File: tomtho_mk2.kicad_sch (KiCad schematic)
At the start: 173 parts, among them J1 USB-C, J2 BATTERY, J3 TRACKPAD, Q1 AO3401A, SW1 SKRAAWE010, SW10 SKRAAWE010, SW11 SKRAAWE010, SW12 SKRAAWE010, SW13 SKRAAWE010, SW14 SKRAAWE010, SW15 SKRAAWE010, SW16 SKRAAWE010, SW17 SKRAAWE010, SW18 SKRAAWE010, SW19 SKRAAWE010, SW2 SKRAAWE010, SW20 SKRAAWE010, SW21 SKRAAWE010, SW22 SKRAAWE010, SW23 SKRAAWE010, SW24 SKRAAWE010, SW25 SKRAAWE010, SW26 SKRAAWE010, SW27 SKRAAWE010, SW28 SKRAAWE010, SW29 SKRAAWE010, SW3 SKRAAWE010, SW30 SKRAAWE010, SW31 SKRAAWE010, SW32 SKRAAWE010, SW33 SKRAAWE010, SW34 SKRAAWE010, SW35 SKRAAWE010, SW36 SKRAAWE010, SW37 SKRAAWE010, SW38 SKRAAWE010, SW39 SKRAAWE010, SW4 SKRAAWE010, SW40 SKRAAWE010, SW41 SKRAAWE010, SW42 SKRAAWE010, SW43 SKRAAWE010, SW44 SKRAAWE010, SW45 SKRAAWE010, SW46 SKRAAWE010, SW47 SKRAAWE010, SW48 SKRAAWE010, SW49 SKRAAWE010, SW5 SKRAAWE010, SW50 SKRAAWE010, SW51 SKRAAWE010, SW52 SKRAAWE010, SW53 SKRAAWE010, SW54 SKRAAWE010, SW55 SKRAAWE010, SW56 SKRAAWE010, SW57 SKRAAWE010, SW58 SKRAAWE010, SW59 SKRAAWE010, SW6 SKRAAWE010, SW60 SKRAAWE010, SW61 SKRAAWE010, SW62 SKRAAWE010, SW63 SKRAAWE010, SW64 SKRAAWE010, SW65 SKRAAWE010, SW66 RESET, SW67 POWER, SW7 SKRAAWE010, SW8 SKRAAWE010, SW9 SKRAAWE010, U1 MDBT50Q-1MV2, U2 USBLC6-2SC6, U3 MCP73831

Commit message: mk2: schematic text layout fixes
Co-Authored-By: Claude Opus 5.5 <noreply@anthropic.com>
Claude-Session: https://claude.ai/code/session_014QKLhpB6tKWk1p8Y7v384p
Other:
- note added: "BT 切替"
- note added: "Battery 1S LiPo (protected)"
- note added: "Charger MCP73831 Ichg = 1000V / R3 = 100 mA LED1 = charging (VBUS powered)"
- note added: "Enter L1"
- note added: "GPIO map (ZMK, diode-direction = col2row) rows: ROW0=P1.10, ROW1=P1.11, ROW2=P1.13, ROW3=P1.15, ROW4=P0.29/AIN5, ROW5=P0.31/AIN7 cols: COL0=P0.30/AIN6, COL1=P0.27, COL2=P0.04/AIN2, COL3=P0.06, COL4=P0.08, COL5=P1.09 COL6=P0.24, COL7=P0.22, COL8=P0.20, COL9=P0.17, COL10=P0.15, COL11=P0.13 LED (active low): LED_BT1=P1.12, LED_BT2=P1.14, LED_BT3=P0.03/AIN1, LED_PWR_G=P0.02/AIN0, LED_PWR_R=P0.28/AIN4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"
- note added: "Indicator LEDs: bicolour, anode = VDD, GPIO sinks (active low) LED2-4 = BT1-3 (green die) / LED5 = power (green OK, red < 20 %)"
- note added: "Load sharing (AN1149) USB -> D66, battery -> Q1 SW67: VSYS -> VDDH"
- note added: "Space L2"
- note added: "Trackpad board (IQS550) FPC 6P 0.5 mm, I2C pull-ups here"
- note added: "tomtho-slim mk2 - 65 keys, roBa-style half stagger, centre trackpad (IQS550 on a separate board) ALPS SKRA 6.2mm / 18.5 x 18 mm pitch / nRF52840 (Raytac MDBT50Q-1MV2, TELEC) / 1S LiPo + USB-C / ZMK"
- note added: "変換 L6"
- note added: "無変換 L3"
- note removed: "BT\n切替"
- note removed: "Battery (1S LiPo, protected cell)"
- note removed: "Charger MCP73831: Ichg = 1000V / R3 = 100 mA\nLED1 lights while charging (VBUS powered)"
- note removed: "Enter\nL1"
- note removed: "GPIO map (ZMK, diode-direction = col2row)\nrows: ROW0=P1.10, ROW1=P1.11, ROW2=P1.13, ROW3=P1.15, ROW4=P0.29/AIN5, ROW5=P0.31/AIN7\ncols: COL0=P0.30/AIN6, COL1=P0.27, COL2=P0.04/AIN2, COL3=P0.06, COL4=P0.08, COL5=P1.09, COL6=P0.24, COL7=P0.22, COL8=P0.20, COL9=P0.17, COL10=P0.15, COL11=P0.13\nLED (active low): LED_BT1=P1.12, LED_BT2=P1.14, LED_BT3=P0.03/AIN1, LED_PWR_G=P0.02/AIN0, LED_PWR_R=P0.28/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"
- note removed: "Indicator LEDs (bicolour, common anode = VDD, GPIO sinks, active low)\nLED2-4 = BT1-3 (green die), LED5 = power (green OK / red < 20 %)"
- note removed: "Load sharing (AN1149): USB -> D66, else battery -> Q1\nPower switch SW67: VSYS -> VDDH"
- note removed: "Space\nL2"
- note removed: "Trackpad board (IQS550) via FPC 6P 0.5 mm, I2C pull-ups on this board"
- note removed: "tomtho-slim mk2 - 65 keys, roBa-style half stagger, centre trackpad (IQS550 on a separate board)\nALPS SKRA 6.2mm / 18.5 x 18 mm pitch / nRF52840 (Raytac MDBT50Q-1MV2, TELEC) / 1S LiPo + USB-C / ZMK"
- note removed: "変換\nL6"
- note removed: "無変換\nL3"

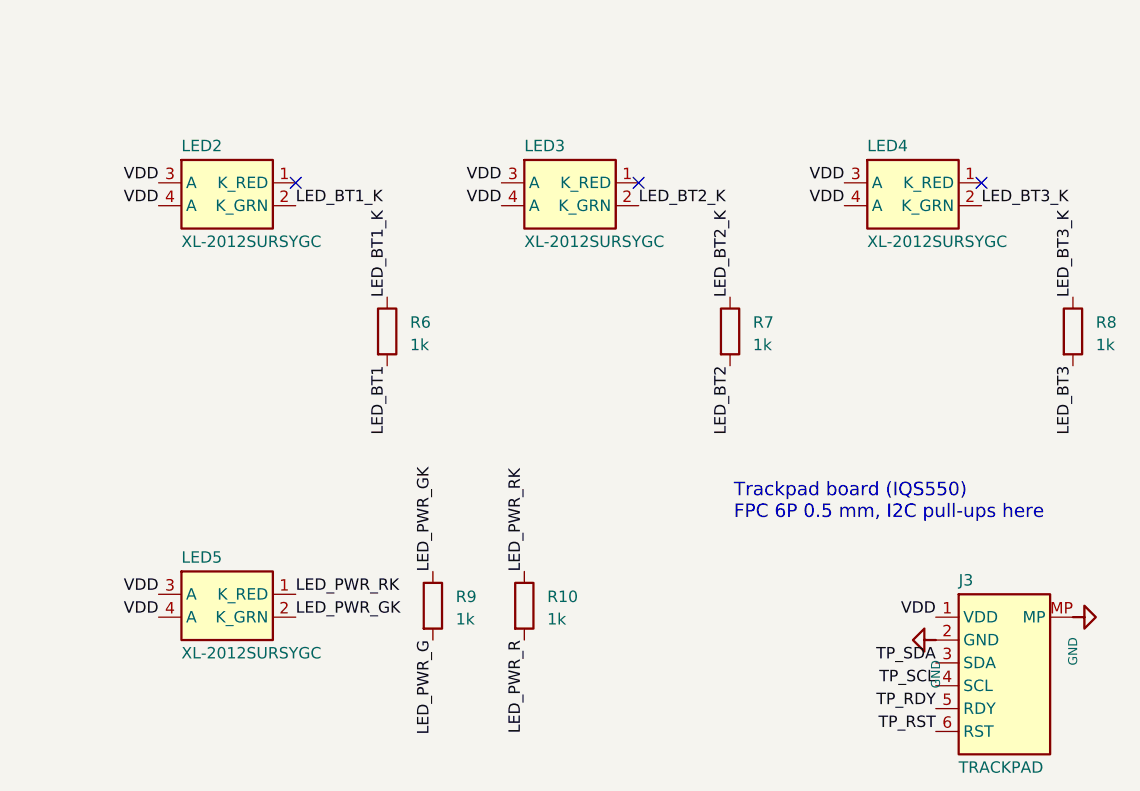
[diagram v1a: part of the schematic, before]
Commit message: mk2: PCB placement (all 173 parts, 0 courtyard overlaps), real LED pin map, top-mount USB-C, local KiCad DRC + Freerouting pipeline
Co-Authored-By: Claude Opus 5.5 <noreply@anthropic.com>
Claude-Session: https://claude.ai/code/session_014QKLhpB6tKWk1p8Y7v384p
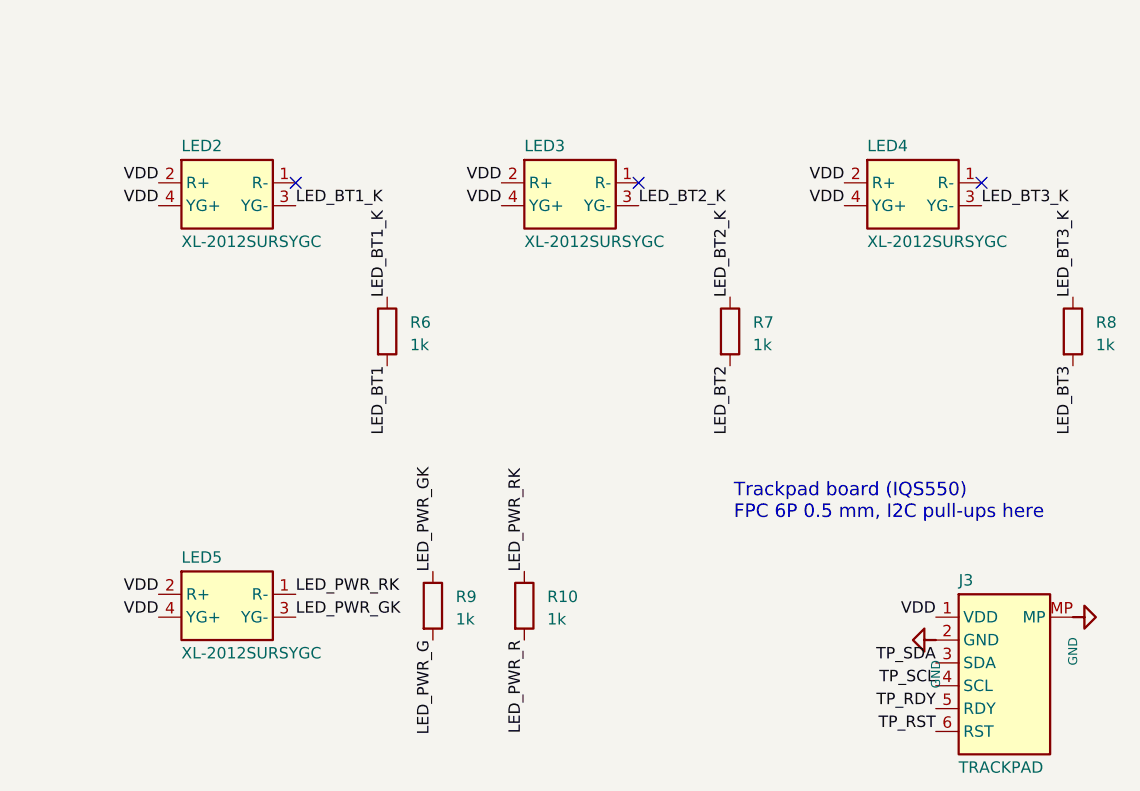
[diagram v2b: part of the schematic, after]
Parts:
- J1: footprint tomtho_mk2:USB_C_SHOUHAN_16P_CB1.6 -> tomtho_mk2:USB_C_HRO_TYPE-C-31-M-12; LCSC C2906290 -> C165948; MPN TYPE-C 16P CB1.6 073 -> TYPE-C-31-M-12
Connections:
- net LED_BT1_K: now also LED2.3 (YG-); no longer LED2.2 (K_GRN)
- net LED_BT2_K: now also LED3.3 (YG-); no longer LED3.2 (K_GRN)
- net LED_BT3_K: now also LED4.3 (YG-); no longer LED4.2 (K_GRN)
- net LED_PWR_GK: now also LED5.3 (YG-); no longer LED5.2 (K_GRN)
- net VDD: now also LED2.2 (R+), LED3.2 (R+), LED4.2 (R+), LED5.2 (R+); no longer LED2.3 (A), LED3.3 (A), LED4.3 (A), LED5.3 (A)
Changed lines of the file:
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@@
 		(property "Reference" "J1" (at 133.35 47.97 0) (effects (font (size 1.27 1.27)) (justify left)))
 		(property "Value" "USB-C" (at 133.35 84.01 0) (effects (font (size 1.27 1.27)) (justify left)))
-		(property "Footprint" "tomtho_mk2:USB_C_SHOUHAN_16P_CB1.6" (at 139.7 66.04 0) (effects (font (size 1.27 1.27)) (hide yes)))
+		(property "Footprint" "tomtho_mk2:USB_C_HRO_TYPE-C-31-M-12" (at 139.7 66.04 0) (effects (font (size 1.27 1.27)) (hide yes)))
 		(property "Datasheet" "~" (at 139.7 66.04 0) (effects (font (size 1.27 1.27)) (hide yes)))
-		(property "Description" "USB2.0 Type-C receptacle, mid-mount (sinks 1.6 mm)" (at 139.7 66.04 0) (effects (font (size 1.27 1.27)) (hide yes)))
-		(property "LCSC" "C2906290" (at 139.7 66.04 0) (effects (font (size 1.27 1.27)) (hide yes)))
-		(property "MPN" "TYPE-C 16P CB1.6 073" (at 139.7 66.04 0) (effects (font (size 1.27 1.27)) (hide yes)))
+		(property "Description" "USB2.0 Type-C receptacle, top mount (sits in the free area under the case top)" (at 139.7 66.04 0) (effects (font (size 1.27 1.27)) (hide yes)))
+		(property "LCSC" "C165948" (at 139.7 66.04 0) (effects (font (size 1.27 1.27)) (hide yes)))
+		(property "MPN" "TYPE-C-31-M-12" (at 139.7 66.04 0) (effects (font (size 1.27 1.27)) (hide yes)))
 		(pin "A4")
 		(pin "A9")
@@
 		(property "LCSC" "C965847" (at 393.7 55.88 0) (effects (font (size 1.27 1.27)) (hide yes)))
 		(property "MPN" "XL-2012SURSYGC" (at 393.7 55.88 0) (effects (font (size 1.27 1.27)) (hide yes)))
-		(pin "3")
+		(pin "2")
 		(pin "4")
 		(pin "1")
-		(pin "2")
+		(pin "3")
 		(instances (project "tomtho_mk2" (path "/cb8fbeca-ed00-5759-aba1-2394e5039438" (reference "LED2") (unit 1))))
 	)
@@
 		(property "LCSC" "C965847" (at 431.8 55.88 0) (effects (font (size 1.27 1.27)) (hide yes)))
 		(property "MPN" "XL-2012SURSYGC" (at 431.8 55.88 0) (effects (font (size 1.27 1.27)) (hide yes)))
-		(pin "3")
+		(pin "2")
 		(pin "4")
 		(pin "1")
-		(pin "2")
+		(pin "3")
 		(instances (project "tomtho_mk2" (path "/cb8fbeca-ed00-5759-aba1-2394e5039438" (reference "LED3") (unit 1))))
 	)
@@
 		(property "LCSC" "C965847" (at 469.9 55.88 0) (effects (font (size 1.27 1.27)) (hide yes)))
 		(property "MPN" "XL-2012SURSYGC" (at 469.9 55.88 0) (effects (font (size 1.27 1.27)) (hide yes)))
-		(pin "3")
+		(pin "2")
 		(pin "4")
 		(pin "1")
-		(pin "2")
+		(pin "3")
 		(instances (project "tomtho_mk2" (path "/cb8fbeca-ed00-5759-aba1-2394e5039438" (reference "LED4") (unit 1))))
 	)
@@
 		(property "LCSC" "C965847" (at 393.7 101.6 0) (effects (font (size 1.27 1.27)) (hide yes)))
 		(property "MPN" "XL-2012SURSYGC" (at 393.7 101.6 0) (effects (font (size 1.27 1.27)) (hide yes)))
-		(pin "3")
+		(pin "2")
 		(pin "4")
 		(pin "1")
-		(pin "2")
+		(pin "3")
 		(instances (project "tomtho_mk2" (path "/cb8fbeca-ed00-5759-aba1-2394e5039438" (reference "LED5") (unit 1))))
 	)

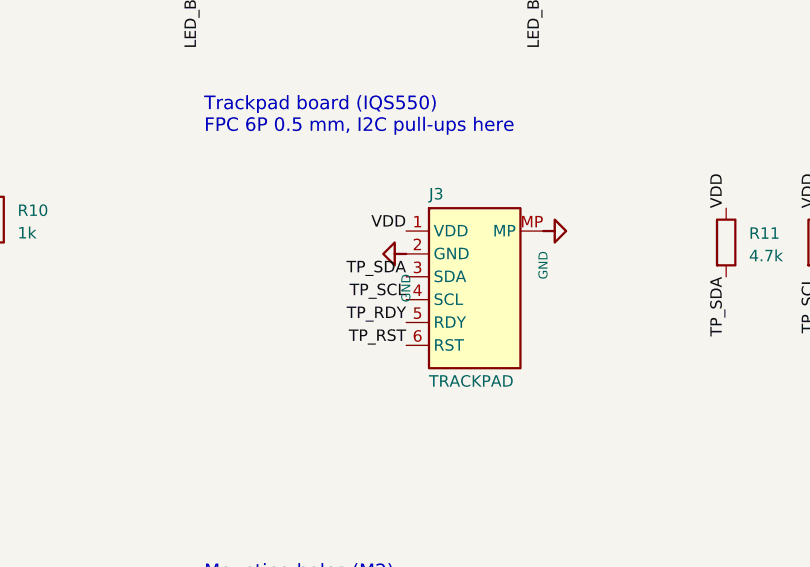
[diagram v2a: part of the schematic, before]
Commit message: mk2: trackpad board derived from GR-Trackpad65 (10Tx x 10Rx, 49x43, DRC clean); main board gets a trackpad cut-out, J3 beside it (DRC 0/0/0)
Co-Authored-By: Claude Opus 5.5 <noreply@anthropic.com>
Claude-Session: https://claude.ai/code/session_014QKLhpB6tKWk1p8Y7v384p
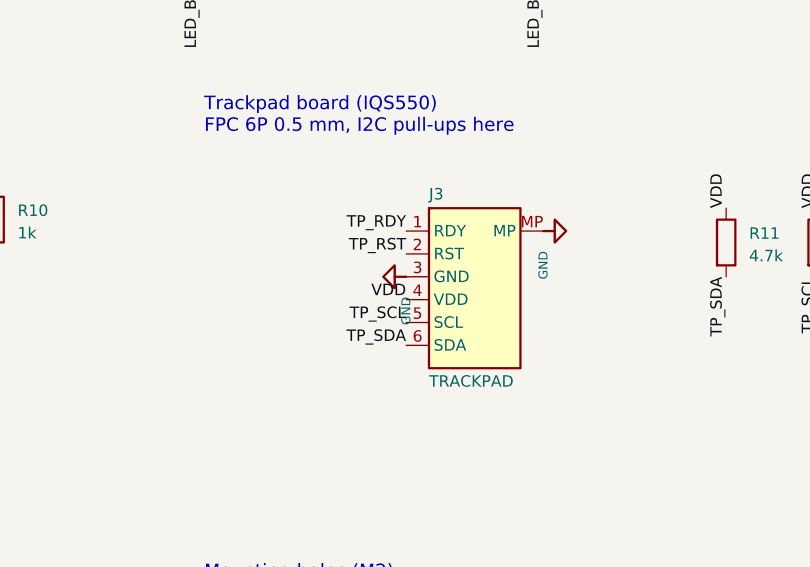
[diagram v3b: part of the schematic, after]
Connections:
- net GND: now also J3.3 (GND); no longer J3.2 (GND)
- net TP_RDY: now also J3.1 (RDY); no longer J3.5 (RDY)
- net TP_RST: now also J3.2 (RST); no longer J3.6 (RST)
- net TP_SCL: now also J3.5 (SCL); no longer J3.4 (SCL)
- net TP_SDA: now also J3.6 (SDA); no longer J3.3 (SDA)
- net VDD: now also J3.4 (VDD); no longer J3.1 (VDD)
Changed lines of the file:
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@@
 		(property "Footprint" "tomtho_mk2:FPC_0.5mm_6P_HC" (at 480.06 109.22 0) (effects (font (size 1.27 1.27)) (hide yes)))
 		(property "Datasheet" "~" (at 480.06 109.22 0) (effects (font (size 1.27 1.27)) (hide yes)))
-		(property "Description" "To IQS550 trackpad board (FPC 6P 0.5 mm)" (at 480.06 109.22 0) (effects (font (size 1.27 1.27)) (hide yes)))
+		(property "Description" "To IQS550 trackpad board (FFC 6P 0.5 mm, type B)" (at 480.06 109.22 0) (effects (font (size 1.27 1.27)) (hide yes)))
 		(property "LCSC" "C5213729" (at 480.06 109.22 0) (effects (font (size 1.27 1.27)) (hide yes)))
 		(property "MPN" "HC-FPC-05-10-6RLTAG" (at 480.06 109.22 0) (effects (font (size 1.27 1.27)) (hide yes)))
@@
 		(instances (project "tomtho_mk2" (path "/cb8fbeca-ed00-5759-aba1-2394e5039438" (reference "J3") (unit 1))))
 	)
-	(label "VDD" (at 472.44 102.87 180) (effects (font (size 1.27 1.27)) (justify right bottom)))
-	(symbol (lib_id "tomtho_mk2:GND") (at 472.44 105.41 270) (unit 1) (exclude_from_sim no) (in_bom no) (on_board no) (dnp no)
-		(property "Reference" "#PWR028" (at 472.44 111.41 0) (effects (font (size 1.27 1.27)) (hide yes)))
-		(property "Value" "GND" (at 472.44 109.21 0) (effects (font (size 1 1))))
-		(property "Footprint" "" (at 472.44 105.41 0) (effects (font (size 1.27 1.27)) (hide yes)))
-		(property "Datasheet" "" (at 472.44 105.41 0) (effects (font (size 1.27 1.27)) (hide yes)))
-		(property "Description" "" (at 472.44 105.41 0) (effects (font (size 1.27 1.27)) (hide yes)))
+	(label "TP_RDY" (at 472.44 102.87 180) (effects (font (size 1.27 1.27)) (justify right bottom)))
+	(label "TP_RST" (at 472.44 105.41 180) (effects (font (size 1.27 1.27)) (justify right bottom)))
+	(symbol (lib_id "tomtho_mk2:GND") (at 472.44 107.95 270) (unit 1) (exclude_from_sim no) (in_bom no) (on_board no) (dnp no)
+		(property "Reference" "#PWR028" (at 472.44 113.95 0) (effects (font (size 1.27 1.27)) (hide yes)))
+		(property "Value" "GND" (at 472.44 111.75 0) (effects (font (size 1 1))))
+		(property "Footprint" "" (at 472.44 107.95 0) (effects (font (size 1.27 1.27)) (hide yes)))
+		(property "Datasheet" "" (at 472.44 107.95 0) (effects (font (size 1.27 1.27)) (hide yes)))
+		(property "Description" "" (at 472.44 107.95 0) (effects (font (size 1.27 1.27)) (hide yes)))
 		(pin "1")
 		(instances (project "tomtho_mk2" (path "/cb8fbeca-ed00-5759-aba1-2394e5039438" (reference "#PWR028") (unit 1))))
 	)
-	(label "TP_SDA" (at 472.44 107.95 180) (effects (font (size 1.27 1.27)) (justify right bottom)))
-	(label "TP_SCL" (at 472.44 110.49 180) (effects (font (size 1.27 1.27)) (justify right bottom)))
-	(label "TP_RDY" (at 472.44 113.03 180) (effects (font (size 1.27 1.27)) (justify right bottom)))
-	(label "TP_RST" (at 472.44 115.57 180) (effects (font (size 1.27 1.27)) (justify right bottom)))
+	(label "VDD" (at 472.44 110.49 180) (effects (font (size 1.27 1.27)) (justify right bottom)))
+	(label "TP_SCL" (at 472.44 113.03 180) (effects (font (size 1.27 1.27)) (justify right bottom)))
+	(label "TP_SDA" (at 472.44 115.57 180) (effects (font (size 1.27 1.27)) (justify right bottom)))
 	(symbol (lib_id "tomtho_mk2:GND") (at 487.68 102.87 90) (unit 1) (exclude_from_sim no) (in_bom no) (on_board no) (dnp no)
 		(property "Reference" "#PWR029" (at 487.68 108.87 0) (effects (font (size 1.27 1.27)) (hide yes)))

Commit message: mk2: trackpad -> Azoteq TPS43-201A-S (43x40); cut-out 44x41, J3 pinout per TPS43 J1; keys unchanged; DRC 0/0/0
Co-Authored-By: Claude Opus 5.5 <noreply@anthropic.com>
Claude-Session: https://claude.ai/code/session_014QKLhpB6tKWk1p8Y7v384p
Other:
- note added: "Trackpad module (Azoteq TPS43) FPC 6P 0.5 mm, I2C pull-ups here"
- note added: "tomtho-slim mk2 - 65 keys, roBa-style half stagger, centre trackpad (Azoteq TPS43 module) ALPS SKRA 6.2mm / 18.5 x 18 mm pitch / nRF52840 (Raytac MDBT50Q-1MV2, TELEC) / 1S LiPo + USB-C / ZMK"
- note removed: "Trackpad board (IQS550) FPC 6P 0.5 mm, I2C pull-ups here"
- note removed: "tomtho-slim mk2 - 65 keys, roBa-style half stagger, centre trackpad (IQS550 on a separate board) ALPS SKRA 6.2mm / 18.5 x 18 mm pitch / nRF52840 (Raytac MDBT50Q-1MV2, TELEC) / 1S LiPo + USB-C / ZMK"
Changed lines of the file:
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@@
 		(date "2026-10-07")
 		(rev "mk2-0.1")
-		(comment 1 "65 keys / ALPS SKRA / MDBT50Q-1MV2 / IQS550 trackpad (FPC) / ZMK")
-	)
-	(text "tomtho-slim mk2  -  65 keys, roBa-style half stagger, centre trackpad (IQS550 on a separate board)\nALPS SKRA 6.2mm / 18.5 x 18 mm pitch / nRF52840 (Raytac MDBT50Q-1MV2, TELEC) / 1S LiPo + USB-C / ZMK" (exclude_from_sim no) (at 20 12 0) (effects (font (size 2 2)) (justify left top)))
+		(comment 1 "65 keys / ALPS SKRA / MDBT50Q-1MV2 / TPS43 trackpad (FPC) / ZMK")
+	)
+	(text "tomtho-slim mk2  -  65 keys, roBa-style half stagger, centre trackpad (Azoteq TPS43 module)\nALPS SKRA 6.2mm / 18.5 x 18 mm pitch / nRF52840 (Raytac MDBT50Q-1MV2, TELEC) / 1S LiPo + USB-C / ZMK" (exclude_from_sim no) (at 20 12 0) (effects (font (size 2 2)) (justify left top)))
 	(text "MCU  (REG0 LDO mode: DCCH open, VDDH = system rail)" (exclude_from_sim no) (at 20 30 0) (effects (font (size 1.5 1.5)) (justify left top)))
 	(symbol (lib_id "tomtho_mk2:MDBT50Q") (at 60.96 101.6 0) (unit 1) (exclude_from_sim no) (in_bom yes) (on_board yes) (dnp no)
@@
 	(label "LED_PWR_RK" (at 426.72 97.79 90) (effects (font (size 1.27 1.27)) (justify left bottom)))
 	(label "LED_PWR_R" (at 426.72 105.41 270) (effects (font (size 1.27 1.27)) (justify right bottom)))
-	(text "Trackpad board (IQS550)\nFPC 6P 0.5 mm, I2C pull-ups here" (exclude_from_sim no) (at 450 88 0) (effects (font (size 1.5 1.5)) (justify left top)))
+	(text "Trackpad module (Azoteq TPS43)\nFPC 6P 0.5 mm, I2C pull-ups here" (exclude_from_sim no) (at 450 88 0) (effects (font (size 1.5 1.5)) (justify left top)))
 	(symbol (lib_id "tomtho_mk2:Conn_FPC6") (at 480.06 109.22 0) (unit 1) (exclude_from_sim no) (in_bom yes) (on_board yes) (dnp no)
 		(property "Reference" "J3" (at 474.98 98.77 0) (effects (font (size 1.27 1.27)) (justify left)))
@@
 		(property "Footprint" "tomtho_mk2:FPC_0.5mm_6P_HC" (at 480.06 109.22 0) (effects (font (size 1.27 1.27)) (hide yes)))
 		(property "Datasheet" "~" (at 480.06 109.22 0) (effects (font (size 1.27 1.27)) (hide yes)))
-		(property "Description" "To IQS550 trackpad board (FFC 6P 0.5 mm, type B)" (at 480.06 109.22 0) (effects (font (size 1.27 1.27)) (hide yes)))
+		(property "Description" "To Azoteq TPS43 trackpad module (FFC 6P 0.5 mm)" (at 480.06 109.22 0) (effects (font (size 1.27 1.27)) (hide yes)))
 		(property "LCSC" "C5213729" (at 480.06 109.22 0) (effects (font (size 1.27 1.27)) (hide yes)))
 		(property "MPN" "HC-FPC-05-10-6RLTAG" (at 480.06 109.22 0) (effects (font (size 1.27 1.27)) (hide yes)))

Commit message: mk2 board check: JLC CPL in Gerber coordinates with per-footprint rotation/origin offsets (verified pad-on-pad against LCSC footprints), charge current 210 mA, README notes (STAT, REGOUT0, battery polarity, MDBT50Q stock)
Co-Authored-By: Claude Opus 5.5 <noreply@anthropic.com>
Claude-Session: https://claude.ai/code/session_014QKLhpB6tKWk1p8Y7v384p
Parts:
- R3: value 10k -> 4.7k; LCSC C25804 -> C23162; MPN 0603WAF1002T5E -> 0603WAF4701T5E
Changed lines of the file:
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@@
 	(symbol (lib_id "tomtho_mk2:R") (at 223.52 76.2 0) (unit 1) (exclude_from_sim no) (in_bom yes) (on_board yes) (dnp no)
 		(property "Reference" "R3" (at 226.06 75.2 0) (effects (font (size 1.27 1.27)) (justify left)))
-		(property "Value" "10k" (at 226.06 77.7 0) (effects (font (size 1.27 1.27)) (justify left)))
+		(property "Value" "4.7k" (at 226.06 77.7 0) (effects (font (size 1.27 1.27)) (justify left)))
 		(property "Footprint" "tomtho_mk2:R_0603" (at 223.52 76.2 0) (effects (font (size 1.27 1.27)) (hide yes)))
 		(property "Datasheet" "~" (at 223.52 76.2 0) (effects (font (size 1.27 1.27)) (hide yes)))
-		(property "Description" "Ichg = 1000V/10k = 100mA" (at 223.52 76.2 0) (effects (font (size 1.27 1.27)) (hide yes)))
-		(property "LCSC" "C25804" (at 223.52 76.2 0) (effects (font (size 1.27 1.27)) (hide yes)))
-		(property "MPN" "0603WAF1002T5E" (at 223.52 76.2 0) (effects (font (size 1.27 1.27)) (hide yes)))
+		(property "Description" "Ichg = 1000V/4.7k = 213mA (0.2-0.5C for an 800-1000 mAh cell)" (at 223.52 76.2 0) (effects (font (size 1.27 1.27)) (hide yes)))
+		(property "LCSC" "C23162" (at 223.52 76.2 0) (effects (font (size 1.27 1.27)) (hide yes)))
+		(property "MPN" "0603WAF4701T5E" (at 223.52 76.2 0) (effects (font (size 1.27 1.27)) (hide yes)))
 		(pin "1")
 		(pin "2")
